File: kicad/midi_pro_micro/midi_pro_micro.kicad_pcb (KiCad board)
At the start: 2 copper layers, 154.5 x 47.5 mm, 28 parts, among them J1 DIN-5_180degree, J2 DIN-5_180degree, J4 Conn_01x16_Pin, SW1 RotaryEncoder_Switch, SW2 SW_Push_LED, SW3 SW_Push_LED, SW4 SW_Push_LED, SW5 SW_Push_LED, U1 ProMicro

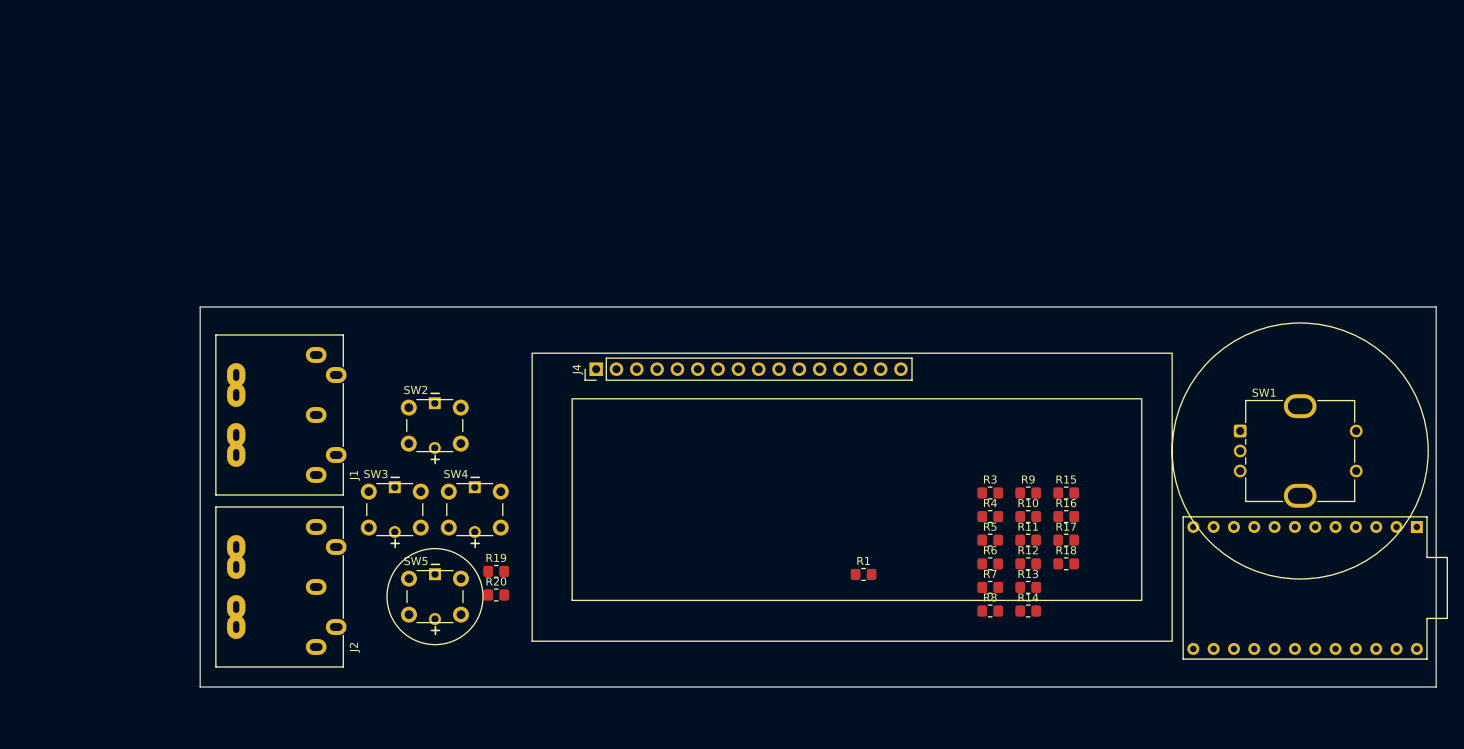
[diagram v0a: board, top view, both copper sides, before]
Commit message: Removing MIDI IN
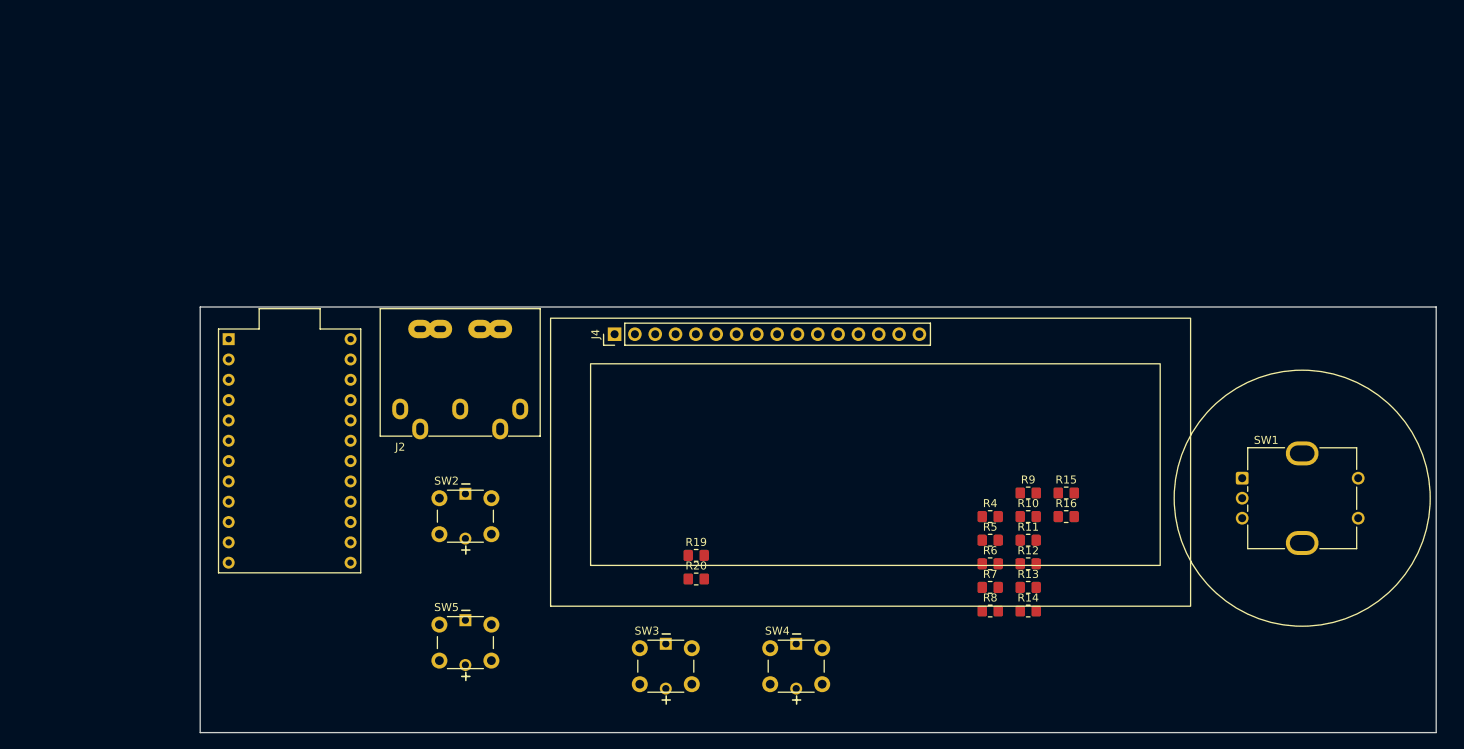
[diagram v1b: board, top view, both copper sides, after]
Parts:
- removed J1: DIN-5_180degree, lib:DIN5MIDI-OOTDTY
- removed R1: R_Small, Resistor_SMD:R_0805_2012Metric_Pad1.20x1.40mm_HandSolder
- removed R17: 470, Resistor_SMD:R_0805_2012Metric_Pad1.20x1.40mm_HandSolder
- removed R18: 10k, Resistor_SMD:R_0805_2012Metric_Pad1.20x1.40mm_HandSolder
- removed R3: 220, Resistor_SMD:R_0805_2012Metric_Pad1.20x1.40mm_HandSolder
- SW2, SW3, SW4, SW5: footprint lib:SW_PUSH_6mm -> lib:SW_PUSH_6mm_LED
- moved U1 128.1 mm to (99.2, 94.5), turned to -90 degrees
- moved SW4 44.7 mm to (159.2, 119.2)
- moved SW3 39.1 mm to (142.9, 119.2)
- moved J2 31.5 mm to (113.0, 89.2), turned to 0 degrees
- moved R19 25.1 mm to (150.0, 107.5)
- moved R20 25.1 mm to (150.0, 110.5)
- moved SW2 12.0 mm to (117.9, 100.4)
- moved SW5 6.89 mm to (117.9, 116.2)
- moved SW1 5.91 mm to (218.2, 97.9)
- moved J4 4.95 mm to (139.8, 79.9)
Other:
- board size 154.5 x 47.5 mm -> 154.5 x 53.2 mm

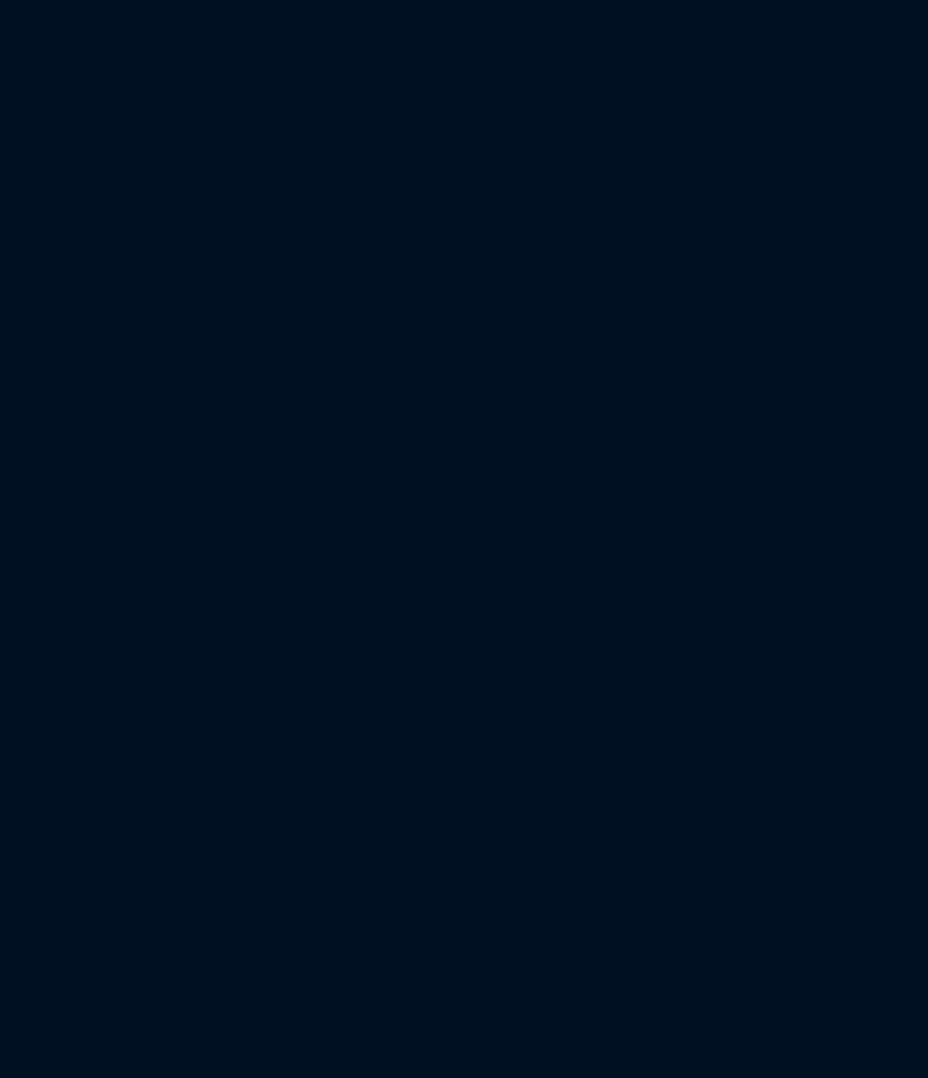
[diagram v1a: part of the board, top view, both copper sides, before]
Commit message: Add MIDI IN once again
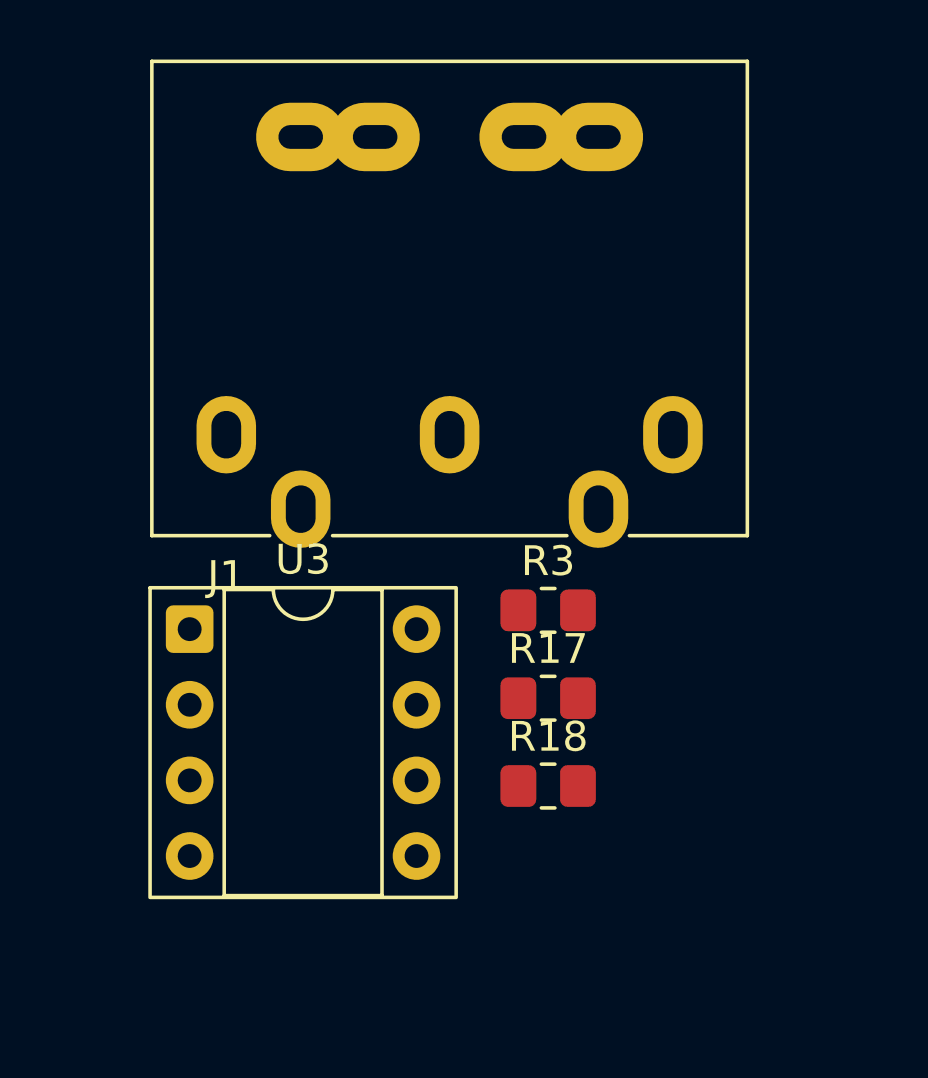
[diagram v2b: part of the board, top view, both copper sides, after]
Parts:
- added J1: DIN-5_180degree, lib:DIN5MIDI-OOTDTY, F.Cu at (93.6, 52.7)
- added R17: 470, Resistor_SMD:R_0805_2012Metric_Pad1.20x1.40mm_HandSolder, F.Cu at (104.4, 61.6)
- added R18: 10k, Resistor_SMD:R_0805_2012Metric_Pad1.20x1.40mm_HandSolder, F.Cu at (104.4, 64.5)
- added R3: 220, Resistor_SMD:R_0805_2012Metric_Pad1.20x1.40mm_HandSolder, F.Cu at (104.4, 58.6)
- added U3: 6N138, Package_DIP:DIP-8_W7.62mm_Socket, F.Cu at (92.3, 59.3)

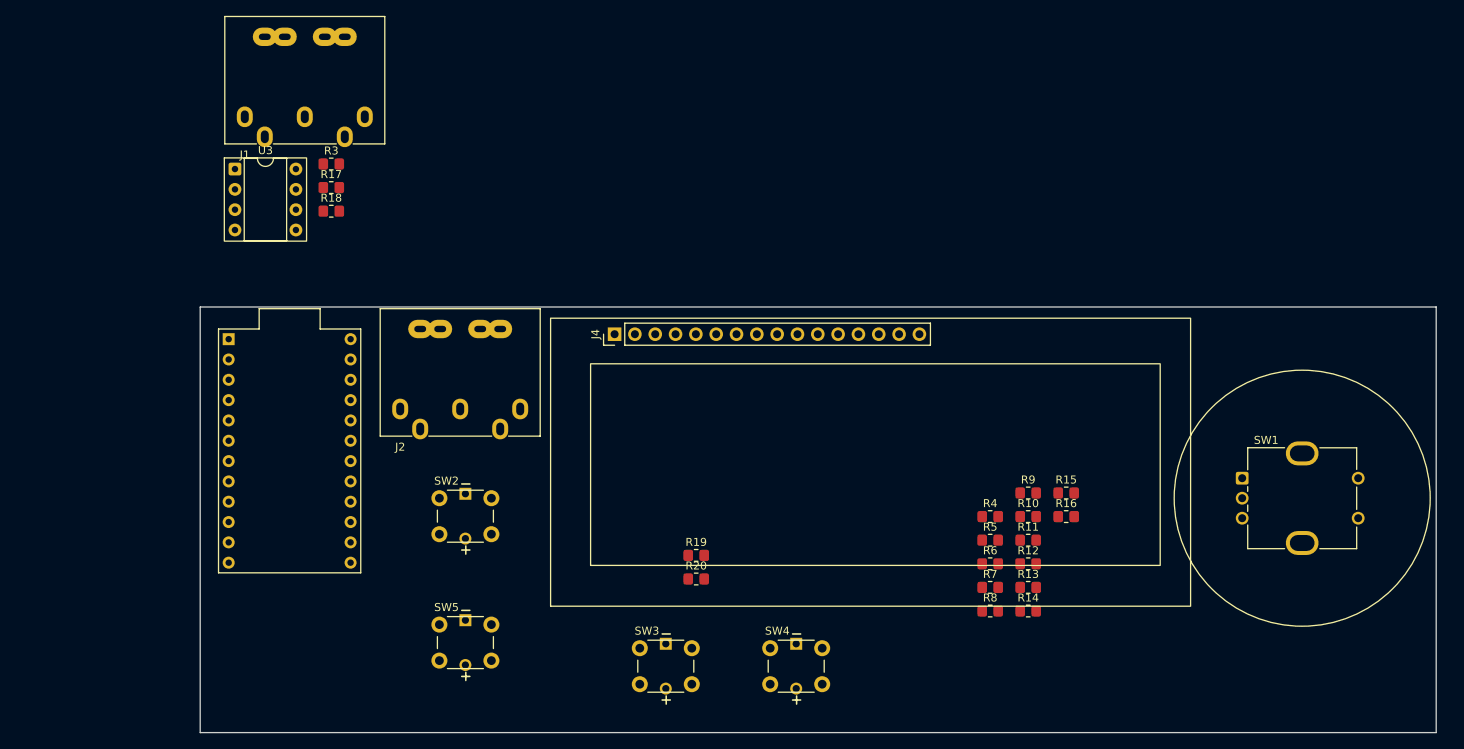
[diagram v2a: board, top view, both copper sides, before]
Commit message: Add 5-way button symbol
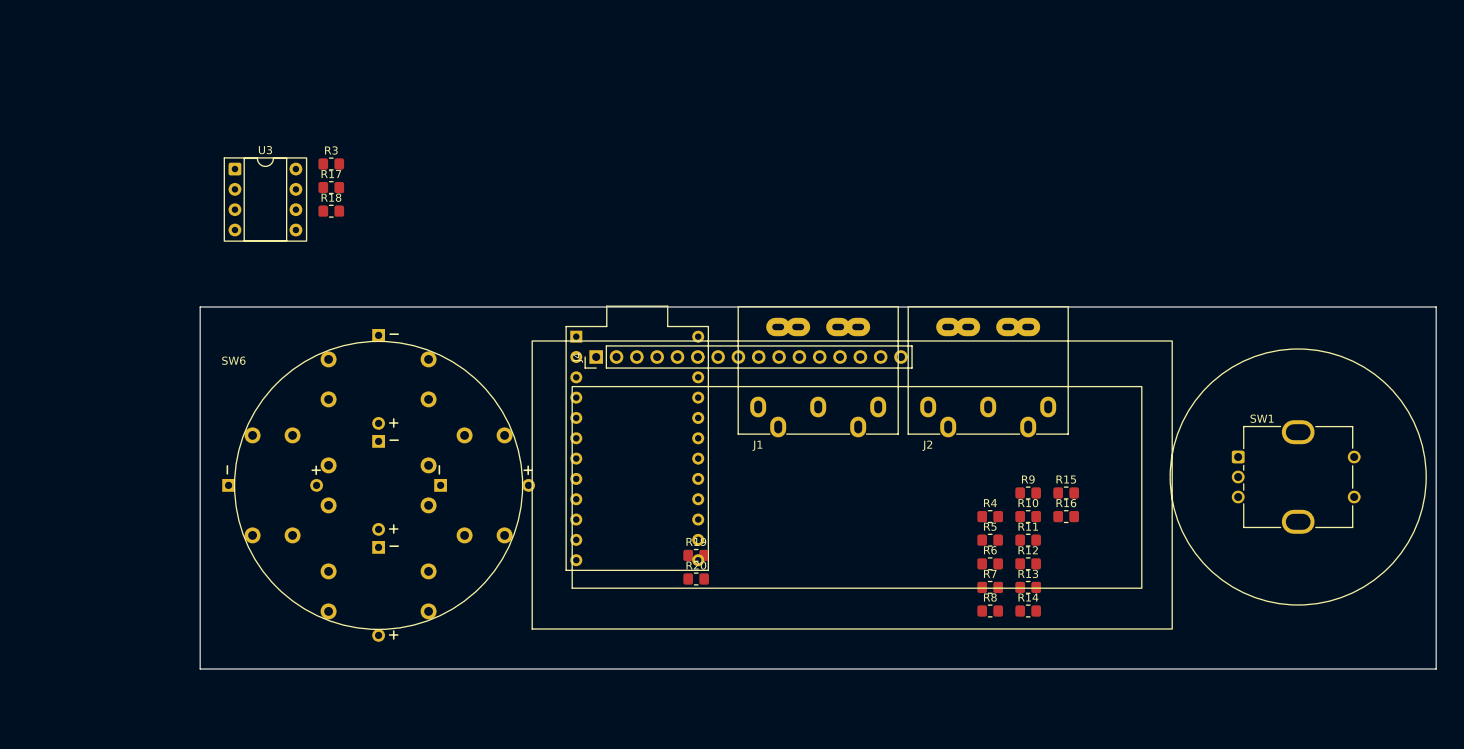
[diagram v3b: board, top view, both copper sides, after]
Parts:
- removed SW2, SW3, SW4, SW5: SW_Push_LED, lib:SW_PUSH_6mm_LED
- added SW6: SW_Push_LEDx5, lib:SW_PUSH_12mm_LEDx5, F.Cu at (110.3, 98.8)
- moved J1 73.7 mm to (157.8, 89.0)
- moved J2 66.0 mm to (179.0, 89.0)
- moved U1 43.5 mm to (142.6, 94.2)
- moved J4 3.66 mm to (137.5, 82.8)
- moved SW1 2.70 mm to (217.8, 95.2)
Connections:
- U1 pad 10: RIGHT_LED -> unconnected-(U1-7,E6-Pad10)
- U1 pad 19: DOWN_LED -> unconnected-(U1-F5,A2,20-Pad19)
- U1 pad 6: LEFT_LED -> unconnected-(U1-3,D0,SCL-Pad6)
- U1 pad 8: UP_LED -> unconnected-(U1-5,C6-Pad8)
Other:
- board size 154.5 x 53.2 mm -> 154.5 x 45.2 mm

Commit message: 5-way-button board
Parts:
- removed R11, R20, R7, R9: 470, Resistor_SMD:R_0805_2012Metric_Pad1.20x1.40mm_HandSolder
- removed SW6: SW_Push_LEDx5, lib:SW_PUSH_12mm_LEDx5
- added J3: Conn_01x12, lib:SW_PUSH_12mm_LEDx5_BOARD, F.Cu at (106.5, 99.0)
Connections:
- net ENC_BTN renamed OK_BTN
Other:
- board size 154.5 x 45.2 mm -> 159.5 x 45.2 mm

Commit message: Add encoder board
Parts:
- removed SW1: RotaryEncoder_Switch, Rotary_Encoder:RotaryEncoder_Bourns_Vertical_PEC12R-3x17F-Sxxxx
- added J6: Conn_01x04, lib:Encoder_BOARD-30x40, F.Cu at (225.6, 99.0)
- moved R19 17.6 mm to (167.5, 109.0)
- moved R4 11.3 mm to (175.5, 101.5)
- moved R5 11.3 mm to (175.5, 105.0)

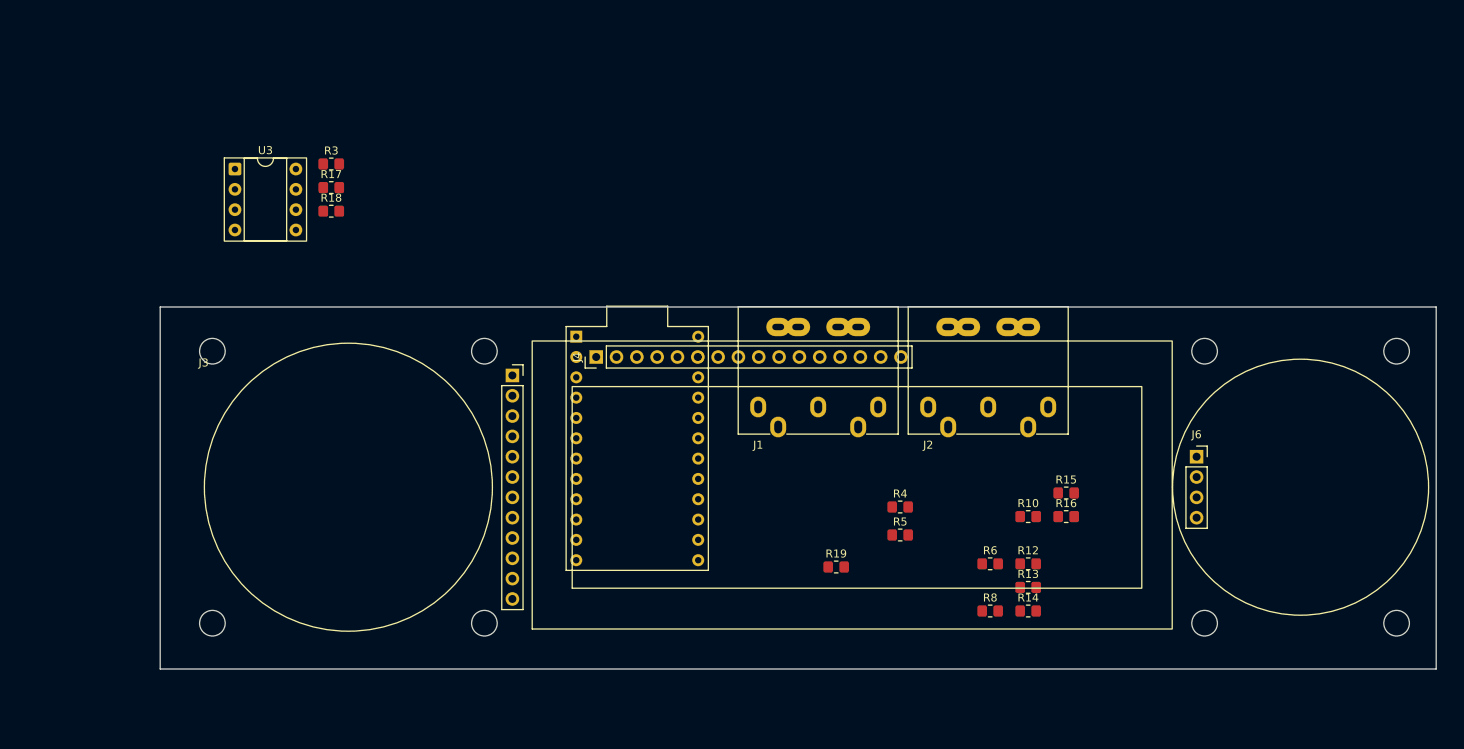
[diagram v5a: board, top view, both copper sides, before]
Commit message: Add 2.42 OLED display
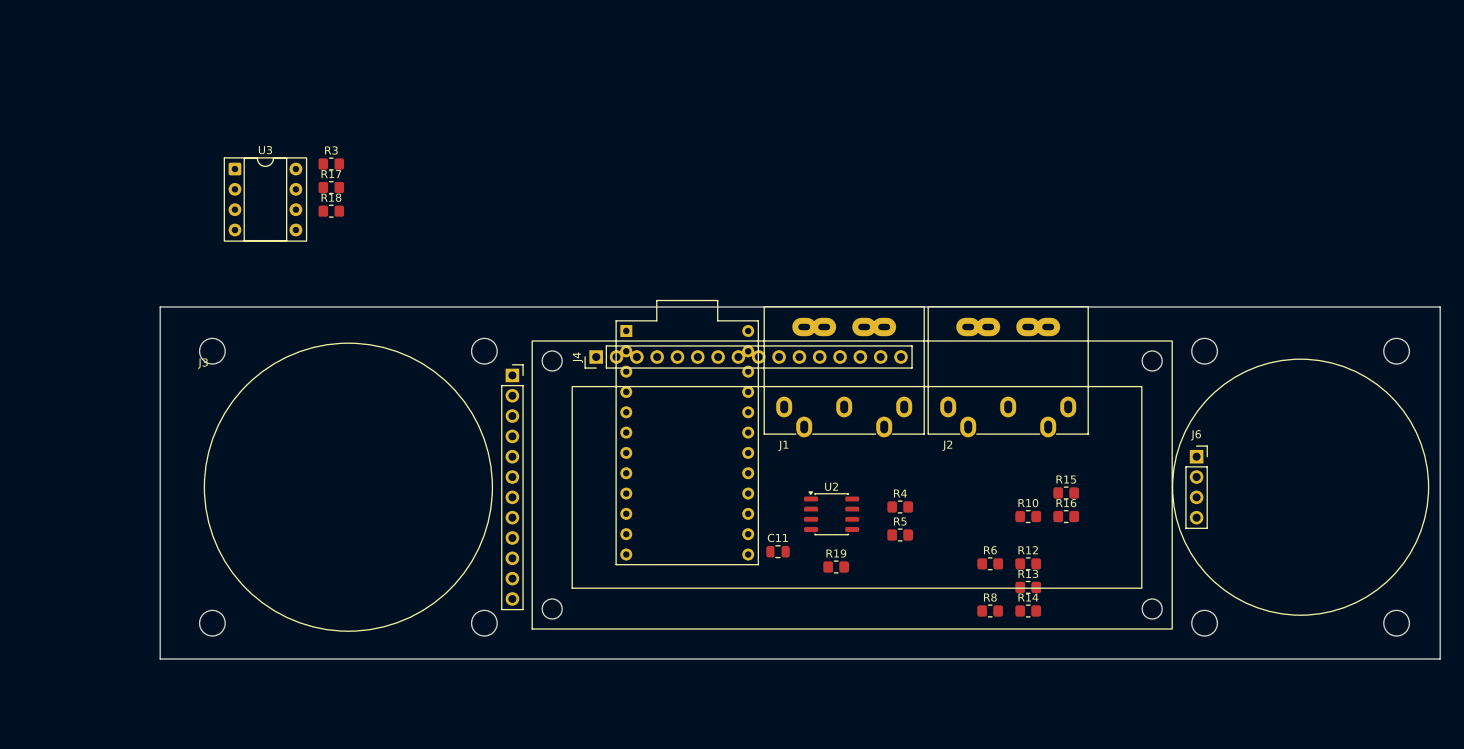
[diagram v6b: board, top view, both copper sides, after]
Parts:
- added C11: 0.1u, Capacitor_SMD:C_0805_2012Metric, F.Cu at (160.2, 107.1)
- added U2: AT25xxx, Package_SO:SO-8_3.9x4.9mm_P1.27mm, F.Cu at (166.9, 102.4)
- moved U1 6.29 mm to (148.9, 93.5)
- moved J1 3.25 mm to (161.0, 89.0)
- moved J2 2.50 mm to (181.5, 89.0)
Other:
- board size 159.5 x 45.2 mm -> 160 x 44 mm
